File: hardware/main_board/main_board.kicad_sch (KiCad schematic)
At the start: 0 parts

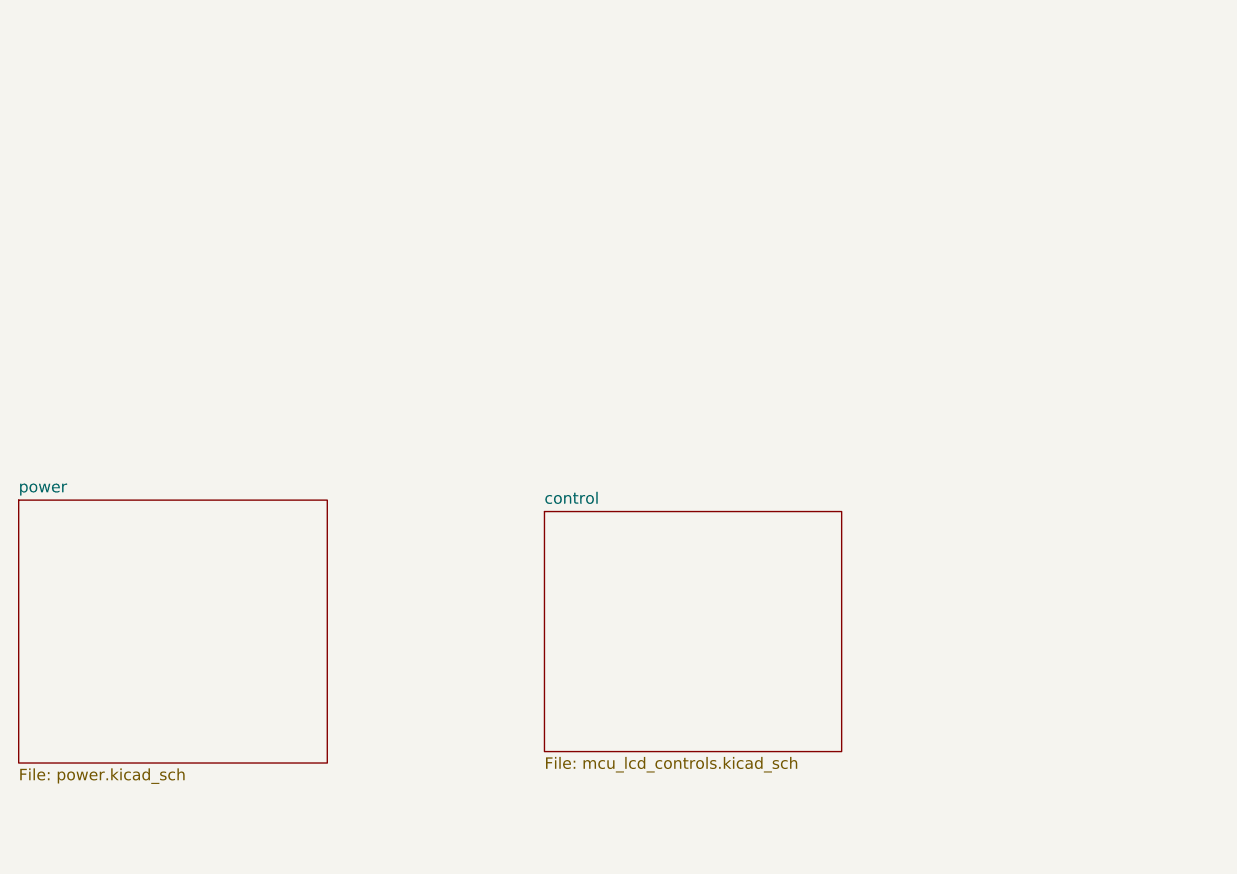
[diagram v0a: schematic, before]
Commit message: Update mainboard schematic to match breadboard
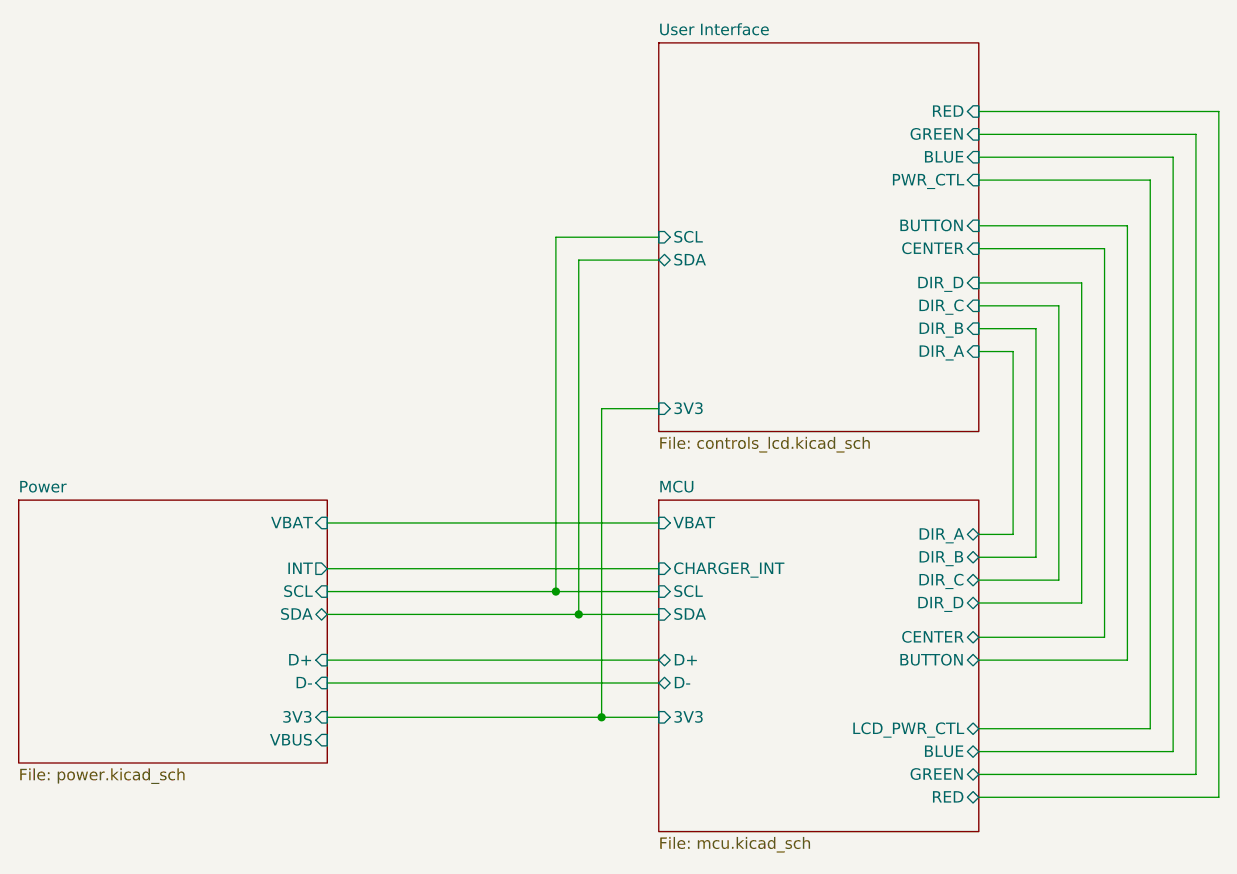
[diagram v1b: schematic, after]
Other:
- sheet power renamed Power
- removed sheet control
- added sheet MCU (mcu.kicad_sch)
- added sheet User Interface (controls_lcd.kicad_sch)
- sheet Power ports: added 3V3, D+, D-, INT, SCL, SDA, VBAT, VBUS; removed none

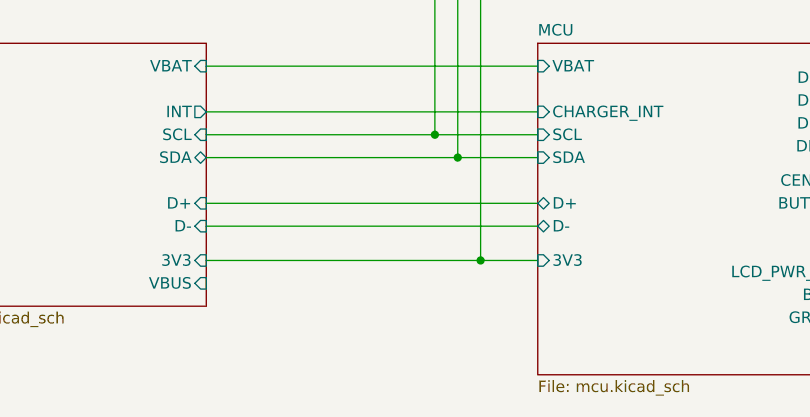
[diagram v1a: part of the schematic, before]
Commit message: Add daughter board connector
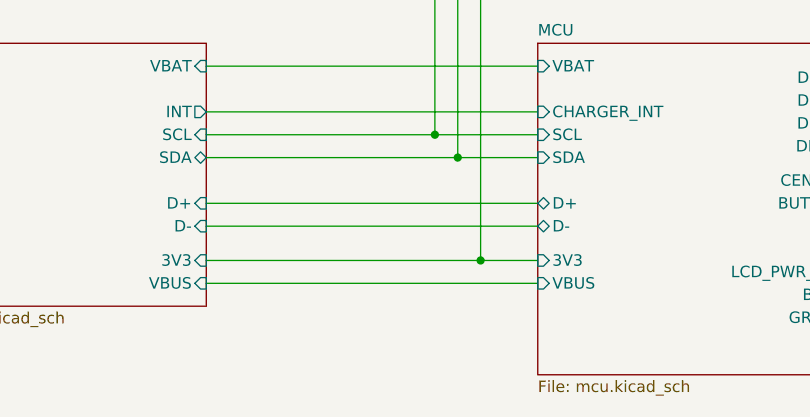
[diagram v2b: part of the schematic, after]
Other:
- sheet MCU ports: added VBUS; removed none
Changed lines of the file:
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@@
+	(wire
+		(pts
+			(xy 63.5 120.65) (xy 100.33 120.65)
+		)
+		(stroke
+			(width 0)
+			(type default)
+		)
+	)
 	(wire
 		(pts
@@
 			(effects
 				(font
+					(size 1.27 1.27)
+				)
+				(justify left)
+			)
+		)
+		(pin "VBUS" input
+			(at 100.33 120.65 180)
+			(effects
+				(font
